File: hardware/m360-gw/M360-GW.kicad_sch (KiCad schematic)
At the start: 17 parts, among them J1 Mezanino M360-RF, J2 5 V ext, J3 LEDs (painel), Q1 2N7002, SW1 Reed, U1 WEMOS D1 mini

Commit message: fix(hardware): GW — correções da revisão adversarial do esquemático
- R1-R3 (LEDs do painel) 1 k -> 470 ohm (C23179): ~3 mA por LED
- R5 100 k (C25803) do MOSI ao GND: com o NSS em LOW desde o power-up,
  transação espúria no rádio vira leitura
- §6: ímã só aciona o modo AP no boot (factory reset não implementado,
  pendência de firmware na §9); janela de sobretensão 6,5-8 V até o PTC
  abrir e fonte travada em 5,0 V; LED verde aceso no boot; corrente do LED
  azul; modo de falha do R4

netdiff: só R5 no MOSI e no GND; campos e lib_symbols conferidos; ERC 0.

Co-Authored-By: Claude Opus 5 (1M context) <noreply@anthropic.com>
Claude-Session: https://claude.ai/code/session_012t7RkcrXvvpDVjKVimNu18
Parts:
- added R5: 100k, Resistor_SMD:R_0603_1608Metric, symbol Device:R
- R1, R2, R3: value 1k -> 470; LCSC C21190 -> C23179
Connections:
- net GND: now also R5.2
- net MOSI: now also R5.1
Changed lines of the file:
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@@
 			)
 		)
-		(property "Value" "1k"
+		(property "Value" "470"
 			(at 39.37 136.906 0)
 			(show_name no)
@@
 			)
 		)
-		(property "LCSC" "C21190"
+		(property "LCSC" "C23179"
 			(at 39.37 134.62 0)
 			(hide yes)
@@
 			)
 		)
-		(property "Value" "1k"
+		(property "Value" "470"
 			(at 39.37 177.546 0)
 			(show_name no)
@@
 			)
 		)
-		(property "LCSC" "C21190"
+		(property "LCSC" "C23179"
 			(at 39.37 175.26 0)
 			(hide yes)
@@
 	)
 	(symbol
+		(lib_id "Device:R")
+		(at 210.820 110.490 0)
+		(unit 1)
+		(body_style 1)
+		(exclude_from_sim no)
+		(in_bom yes)
+		(on_board yes)
+		(in_pos_files yes)
+		(dnp no)
+		(property "Reference" "R5"
+			(at 208.788 110.236 90)
+			(show_name no)
+			(do_not_autoplace no)
+			(effects
+				(font
+					(size 1.27 1.27)
+				)
+			)
+		)
+		(property "Value" "100k"
+			(at 213.106 110.236 90)
+			(show_name no)
+			(do_not_autoplace no)
+			(effects
+				(font
+					(size 1.27 1.27)
+				)
+			)
+		)
+		(property "Footprint" "Resistor_SMD:R_0603_1608Metric"
+			(at 209.042 110.490 90)
+			(hide yes)
+			(show_name no)
+			(do_not_autoplace no)
+			(effects
+				(font
+					(size 1.27 1.27)
+				)
+			)
+		)
+		(property "Datasheet" ""
+			(at 210.820 110.490 0)
+			(hide yes)
+			(show_name no)
+			(do_not_autoplace no)
+			(effects
+				(font
+					(size 1.27 1.27)
+				)
+			)
+		)
+		(property "Description" "Resistor"
+			(at 210.820 110.490 0)
+			(hide yes)
+			(show_name no)
+			(do_not_autoplace no)
+			(effects
+				(font
+					(size 1.27 1.27)
+				)
+			)
+		)
+		(property "LCSC" "C25803"
+			(at 210.820 110.490 0)
+			(hide yes)
+			(show_name no)
+			(do_not_autoplace no)
+			(effects
+				(font
+					(size 1.27 1.27)
+				)
+			)
+		)
+		(pin "1"
+		)
+		(pin "2"
+		)
+		(instances
+			(project "M360-GW"
+				(path "/48a18d9a-df80-4072-896a-d7ca09082424"
+					(reference "R5")
+					(unit 1)
+				)
+			)
+		)
+	)
+	(wire
+		(pts
+			(xy 210.82 106.68) (xy 210.82 102.87)
+		)
+		(stroke
+			(width 0)
+			(type default)
+		)
+	)
+	(label "MOSI"
+		(at 210.82 102.87 90)
+		(effects
+			(font
+				(size 1.27 1.27)
+			)
+			(justify left bottom)
+		)
+	)
+	(wire
+		(pts
+			(xy 210.82 114.3) (xy 210.82 118.11)
+		)
+		(stroke
+			(width 0)
+			(type default)
+		)
+	)
+	(label "GND"
+		(at 210.82 118.11 270)
+		(effects
+			(font
+				(size 1.27 1.27)
+			)
+			(justify right bottom)
+		)
+	)
+	(symbol
 		(lib_id "Device:Polyfuse")
 		(at 114.3 38.1 0)
@@
 			)
 		)
-		(property "Value" "1k"
+		(property "Value" "470"
 			(at 39.37 157.226 0)
 			(show_name no)
@@
 			)
 		)
-		(property "LCSC" "C21190"
+		(property "LCSC" "C23179"
 			(at 39.37 154.94 0)
 			(hide yes)

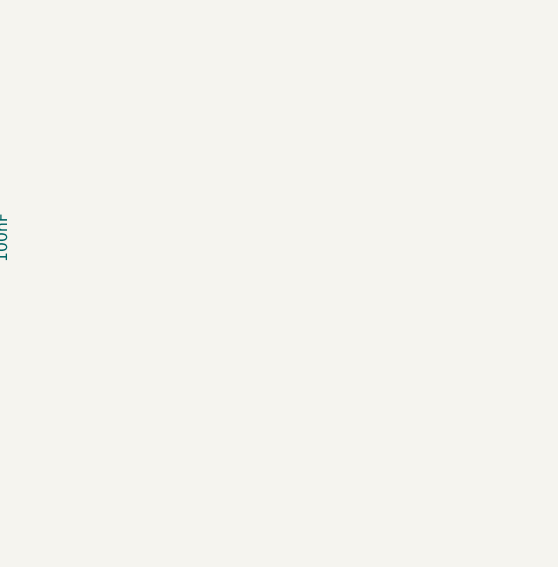
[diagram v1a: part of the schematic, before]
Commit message: feat(hardware): header 1x8 do nRF24 legado nas placas GW, LP e ACT
- esquemáticos: header 1x8 "nRF24 legado" (GW J4, LP J5, ACT J6; C492407,
  solda manual, fora do BOM e da posição) e 10 uF 0805 (C5/C16/C9, C15850)
  nas mesmas redes do soquete do mezanino: CE = DIO0, CSN = NSS, IRQ = DIO1
  (sem ligação na GW). Um rádio por placa: nRF24 OU mezanino RFM95W
- tools/add_nrf_header.py: grava símbolo, fios e labels por texto, embute o
  Conn_01x08 stock e confere colisão; netdiff só nas redes previstas, ERC 0,
  campos e lib_symbols inalterados nas três folhas
- placas rerroteadas sem apagar a fiação existente (DSN com fios fixos e
  cobertos por área proibida, mais áreas proibidas sobre os fiduciais);
  vias de GND junto do pino 8 e do capacitor; legenda "nRF24 OU mezanino"
  e "CE" no pino 1. GW 287 trilhas/43 vias, LP 855/135, ACT 939/141;
  DRC --severity-all 0/0, paridade idêntica, ordem_tvs 13/13 e 15/15
- fabricacao/ regerada: GW 15, LP 53, ACT 54 peças
- ARQUITETURA §2 (decisão 15), §4.2, §5.2, §6.1, §8, §9, §9.1; datasheet
  C492407 em docs/datasheets. Firmware pendente: MY_RF24_CE_PIN=5 (GW) e
  =2 (LP/ACT), a testar na bancada

Co-Authored-By: Claude Fable 5.1 <noreply@anthropic.com>
Claude-Session: https://claude.ai/code/session_01M8U92DFNnZt7SqLtzrKYSR
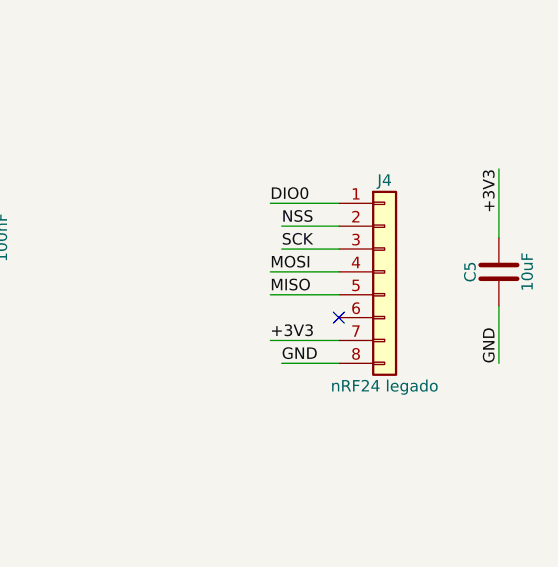
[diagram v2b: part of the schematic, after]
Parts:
- added C5: 10uF, Capacitor_SMD:C_0805_2012Metric, symbol Device:C
- added J4: nRF24 legado, Connector_PinHeader_2.54mm:PinHeader_1x08_P2.54mm_Vertical, symbol Connector_Generic:Conn_01x08
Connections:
- net +3V3: now also C5.1, J4.7 (Pin_7)
- net DIO0: now also J4.1 (Pin_1)
- net GND: now also C5.2, J4.8 (Pin_8)
- net MISO: now also J4.5 (Pin_5)
- net MOSI: now also J4.4 (Pin_4)
- net NSS: now also J4.2 (Pin_2)
- net SCK: now also J4.3 (Pin_3)
- no-connect marks 6 -> 7
